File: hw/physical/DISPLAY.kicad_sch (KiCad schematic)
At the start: 0 parts

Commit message: - Consolidate POWER and BATTERY pages - Updated 1.8V SYS REG to low Iq option - Replaced LoRA module with SemTech transceiver - Adding latest nRF datasheet
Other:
- note added: "TBD"
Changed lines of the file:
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@@
 		(comment 1 "Brendan Bleker")
 	)
+	(text "TBD"
+		(exclude_from_sim no)
+		(at 220.98 129.794 0)
+		(effects
+			(font
+				(size 2.54 2.54)
+				(color 255 21 0 1)
+			)
+		)
+	)
 )

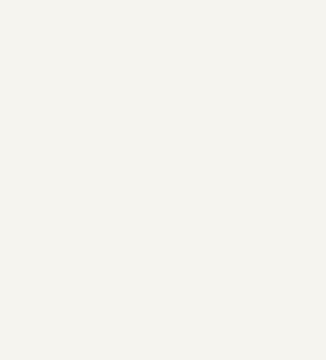
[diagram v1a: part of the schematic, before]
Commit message: Adding nRF54L10 schematic library component. Redrew MCU page with nRF54L10 and rearranged or changed net labels and global labels.
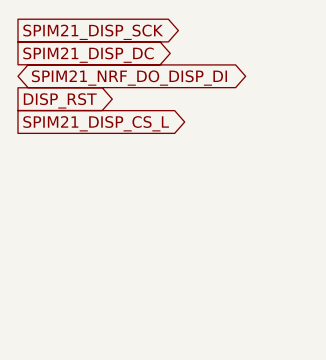
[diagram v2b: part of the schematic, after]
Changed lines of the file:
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@@
+		)
+	)
+	(global_label "SPIM21_DISP_SCK"
+		(shape output)
+		(at 193.04 80.01 0)
+		(fields_autoplaced yes)
+		(effects
+			(font
+				(size 1.27 1.27)
+			)
+			(justify left)
+		)
+		(property "Intersheetrefs" "${INTERSHEET_REFS}"
+			(at 213.0189 80.01 0)
+			(effects
+				(font
+					(size 1.27 1.27)
+				)
+				(justify left)
+				(hide yes)
+			)
+		)
+	)
+	(global_label "SPIM21_NRF_DO_DISP_DI"
+		(shape bidirectional)
+		(at 193.04 85.09 0)
+		(fields_autoplaced yes)
+		(effects
+			(font
+				(size 1.27 1.27)
+			)
+			(justify left)
+		)
+		(property "Intersheetrefs" "${INTERSHEET_REFS}"
+			(at 220.4803 85.09 0)
+			(effects
+				(font
+					(size 1.27 1.27)
+				)
+				(justify left)
+				(hide yes)
+			)
+		)
+	)
+	(global_label "SPIM21_DISP_DC"
+		(shape output)
+		(at 193.04 82.55 0)
+		(fields_autoplaced yes)
+		(effects
+			(font
+				(size 1.27 1.27)
+			)
+			(justify left)
+		)
+		(property "Intersheetrefs" "${INTERSHEET_REFS}"
+			(at 211.8094 82.55 0)
+			(effects
+				(font
+					(size 1.27 1.27)
+				)
+				(justify left)
+				(hide yes)
+			)
+		)
+	)
+	(global_label "DISP_RST"
+		(shape output)
+		(at 193.04 87.63 0)
+		(fields_autoplaced yes)
+		(effects
+			(font
+				(size 1.27 1.27)
+			)
+			(justify left)
+		)
+		(property "Intersheetrefs" "${INTERSHEET_REFS}"
+			(at 204.7942 87.63 0)
+			(effects
+				(font
+					(size 1.27 1.27)
+				)
+				(justify left)
+				(hide yes)
+			)
+		)
+	)
+	(global_label "SPIM21_DISP_CS_L"
+		(shape output)
+		(at 193.04 90.17 0)
+		(fields_autoplaced yes)
+		(effects
+			(font
+				(size 1.27 1.27)
+			)
+			(justify left)
+		)
+		(property "Intersheetrefs" "${INTERSHEET_REFS}"
+			(at 213.7446 90.17 0)
+			(effects
+				(font
+					(size 1.27 1.27)
+				)
+				(justify left)
+				(hide yes)
+			)
 		)
 	)

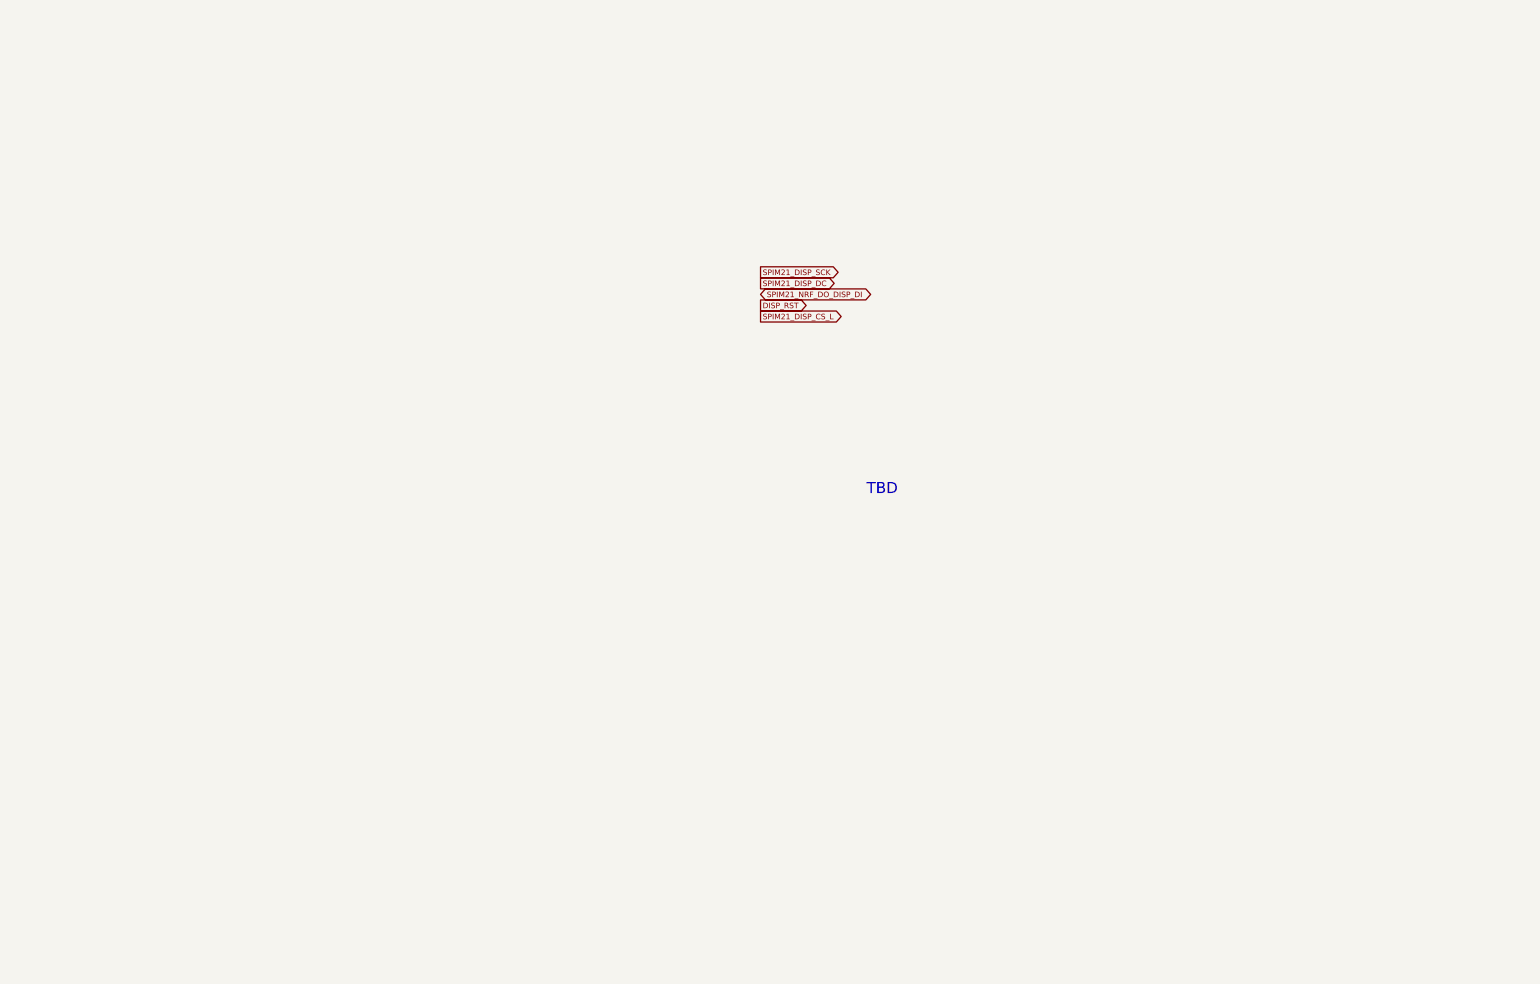
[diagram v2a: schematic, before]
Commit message: Various Schematic Modifications and Additions. * Removed Bypass page and moved bypass caps to MCU page. * Moved MCU VSS_PA pin to logical location as per Nordic guidelines. * Added Display Circuit, level shifters, charge pump, connector, etc. * Added 3.3V display VREG with Enable GPIO. * Added BLE RF components as per Nordic guidelines. * Added DCC circuit as per Nordic guidelines. * Rearranged GPIO's and interfaces. * Fixed various schematic errors.
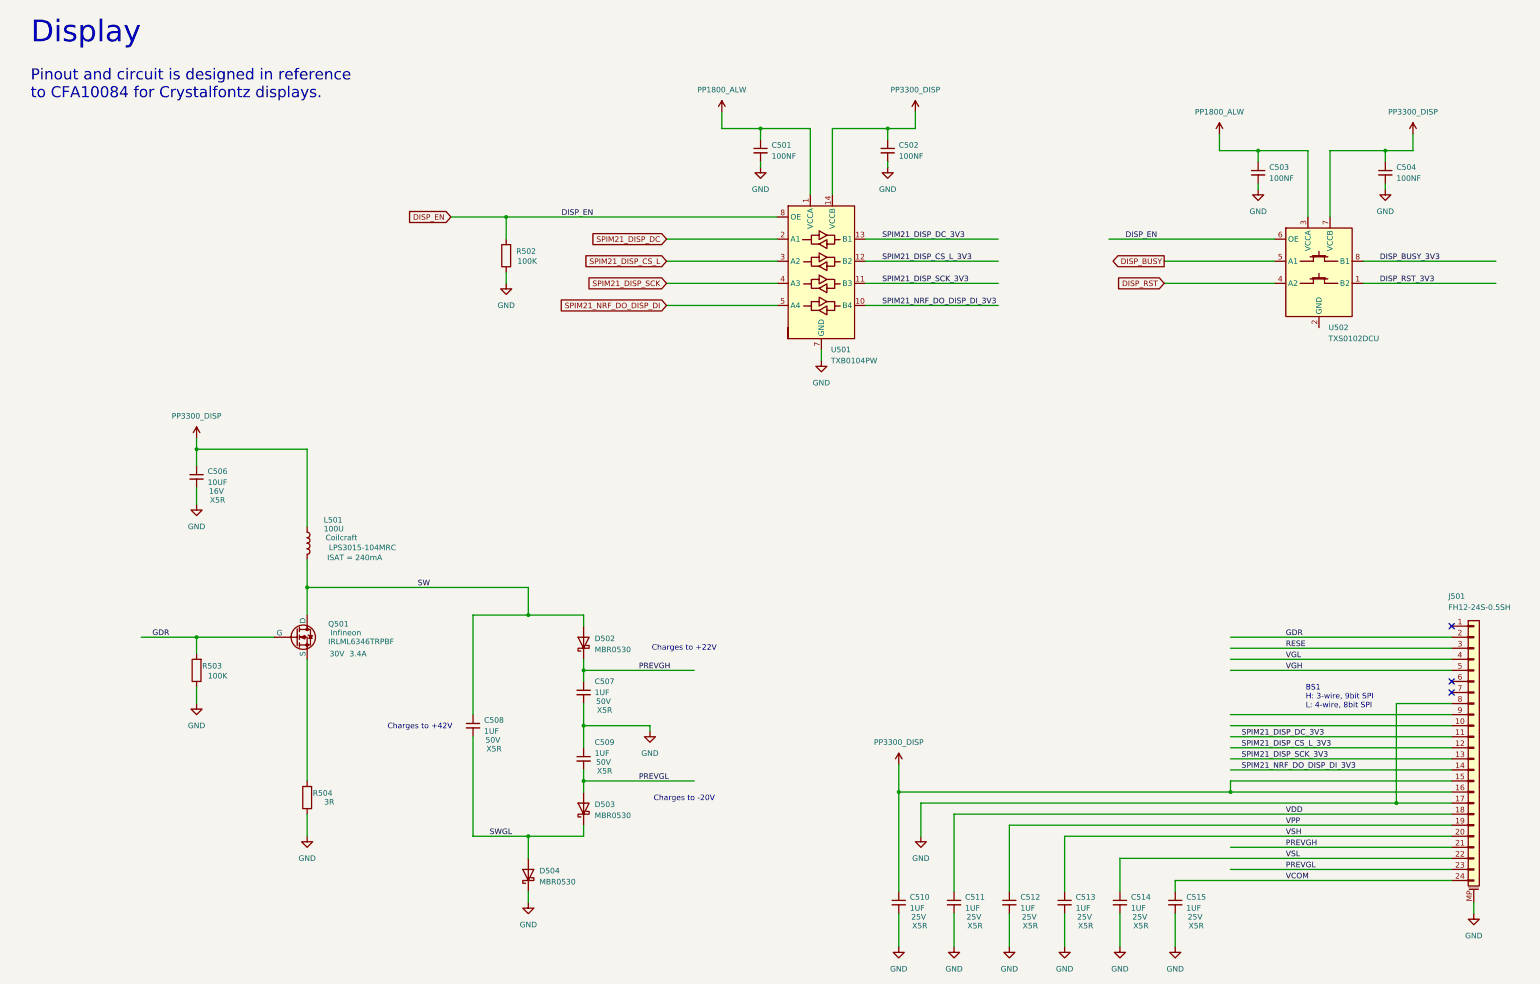
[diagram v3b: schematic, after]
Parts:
- added C501, C502, C503, C504: 100NF, symbol Device:C_Small
- added C506: 10UF, symbol Device:C_Small
- added C507, C508, C509, C510, C511, C512, C513, C514, C515: 1UF, symbol Device:C_Small
- added D502, D503, D504: MBR0530, Diode_SMD:D_SOD-123, symbol Diode:MBR0530
- added J501: FH12-24S-0.5SH, Connector_FFC-FPC:Hirose_FH12-24S-0.5SH_1x24-1MP_P0.50mm_Horizontal, symbol Connector_Generic_MountingPin:Conn_01x24_MountingPin
- added L501: 100U, symbol Device:L
- added Q501: IRLML6346TRPBF, Package_TO_SOT_SMD:SOT-23, symbol Simulation_SPICE:NMOS
- added R502, R503: 100K, symbol Device:R
- added R504: 3R, symbol Device:R
- added U501: TXB0104PW, Package_SO:TSSOP-14_4.4x5mm_P0.65mm, symbol Logic_LevelTranslator:TXB0104PW
- added U502: TXS0102DCU, Package_SO:VSSOP-8_2.3x2mm_P0.5mm, symbol Logic_LevelTranslator:TXS0102DCU
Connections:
- net DISP_RST: now also U502.4 (A2)
- net SPIM21_DISP_CS_L: now also U501.3 (A2)
- net SPIM21_DISP_DC: now also U501.2 (A1)
- net SPIM21_DISP_SCK: now also U501.4 (A3)
- net SPIM21_NRF_DO_DISP_DI: now also U501.5 (A4)
- new net: Q501.3 (S), R504.2
- new net DISP_BUSY: U502.5 (A1)
- new net DISP_BUSY_3V3: U502.8 (B1)
- new net DISP_EN: R502.2, U501.8 (OE), U502.6 (OE)
- new net DISP_RST_3V3: U502.1 (B2)
- new net GDR: J501.2 (Pin_2), Q501.2 (G), R503.2
- new net GND: C501.2, C502.2, C503.2, C504.2, C506.2, C507.2, C509.1, C510.2, C511.2, C512.2, C513.2, C514.2, C515.2, D504.1 (K), J501.17 (Pin_17), J501.8 (Pin_8), J501.MP (MountPin), R502.1, R503.1, R504.1, U501.7 (GND)
- new net PP1800_ALW: C501.1, C503.1, U501.1 (VCCA), U502.3 (VCCA)
- new net PP3300_DISP: C502.1, C504.1, C506.1, C510.1, J501.15 (Pin_15), J501.16 (Pin_16), L501.1, U501.14 (VCCB), U502.7 (VCCB)
- new net PREVGH: C507.1, D502.1 (K), J501.21 (Pin_21)
- new net PREVGL: C509.2, D503.2 (A), J501.23 (Pin_23)
- new net RESE: J501.3 (Pin_3)
- new net SPIM21_DISP_CS_L_3V3: J501.12 (Pin_12), U501.12 (B2)
- new net SPIM21_DISP_DC_3V3: J501.11 (Pin_11), U501.13 (B1)
- new net SPIM21_DISP_SCK_3V3: J501.13 (Pin_13), U501.11 (B3)
- new net SPIM21_NRF_DO_DISP_DI_3V3: J501.14 (Pin_14), U501.10 (B4)
- new net SW: C508.1, D502.2 (A), L501.2, Q501.1 (D)
- new net SWGL: C508.2, D503.1 (K), D504.2 (A)
- new net VCOM: C515.1, J501.24 (Pin_24)
- new net VDD: C511.1, J501.18 (Pin_18)
- new net VGH: J501.5 (Pin_5)
- new net VGL: J501.4 (Pin_4)
- new net VPP: C512.1, J501.19 (Pin_19)
- new net VSH: C513.1, J501.20 (Pin_20)
- new net VSL: C514.1, J501.22 (Pin_22)
- no-connect marks 0 -> 3
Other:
- note added: "BS1 H: 3-wire, 9bit SPI L: 4-wire, 8bit SPI"
- note added: "Charges to +22V"
- note added: "Charges to +42V"
- note added: "Charges to -20V"
- note added: "Display"
- note added: "Pinout and circuit is designed in reference to CFA10084 for Crystalfontz displays."
- note removed: "TBD"
